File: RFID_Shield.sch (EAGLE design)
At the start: 8 parts, among them J1 ARDUINO_R3_SHIELD, Q1 MMBT2222, U1 RFID

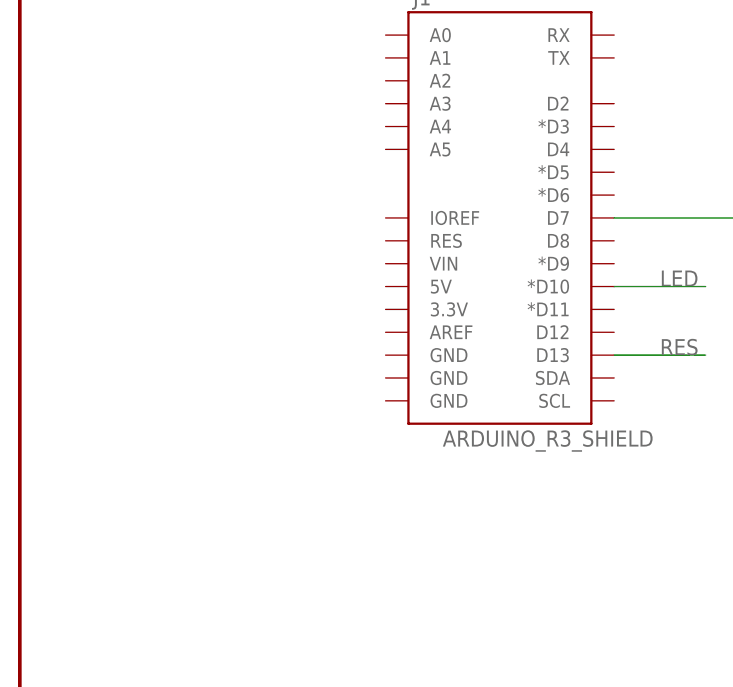
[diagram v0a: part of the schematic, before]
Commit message: Fixed missing VCC and GND connections.
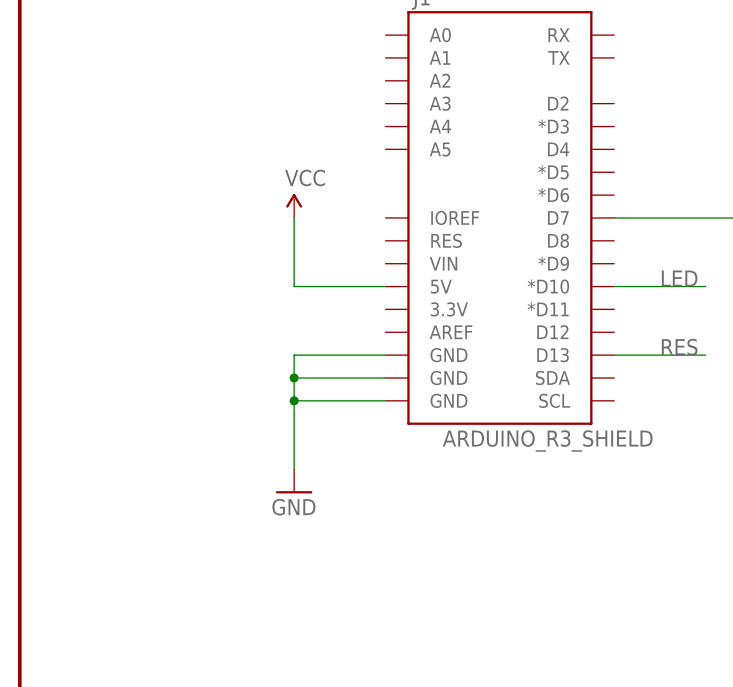
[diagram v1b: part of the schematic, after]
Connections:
- net GND: now also J1.GND@0, J1.GND@1, J1.GND@2
- net VCC: now also J1.5V
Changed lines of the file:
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@@
 <part name="GND1" library="SparkFun-Aesthetics" deviceset="GND" device=""/>
 <part name="GND2" library="SparkFun-Aesthetics" deviceset="GND" device=""/>
+<part name="SUPPLY2" library="SparkFun-Aesthetics" deviceset="VCC" device=""/>
+<part name="GND3" library="SparkFun-Aesthetics" deviceset="GND" device=""/>
 </parts>
 <sheets>
@@
 <instance part="GND1" gate="1" x="182.88" y="124.46" rot="R180"/>
 <instance part="GND2" gate="1" x="152.4" y="104.14"/>
+<instance part="SUPPLY2" gate="G$1" x="73.66" y="116.84"/>
+<instance part="GND3" gate="1" x="73.66" y="86.36"/>
 </instances>
 <busses>
@@
 <wire x1="182.88" y1="119.38" x2="182.88" y2="121.92" width="0.1524" layer="91"/>
 </segment>
+<segment>
+<pinref part="J1" gate="G$1" pin="GND@2"/>
+<pinref part="GND3" gate="1" pin="GND"/>
+<wire x1="83.82" y1="101.6" x2="73.66" y2="101.6" width="0.1524" layer="91"/>
+<wire x1="73.66" y1="101.6" x2="73.66" y2="99.06" width="0.1524" layer="91"/>
+<pinref part="J1" gate="G$1" pin="GND@1"/>
+<wire x1="73.66" y1="99.06" x2="73.66" y2="96.52" width="0.1524" layer="91"/>
+<wire x1="73.66" y1="96.52" x2="73.66" y2="88.9" width="0.1524" layer="91"/>
+<wire x1="83.82" y1="99.06" x2="73.66" y2="99.06" width="0.1524" layer="91"/>
+<junction x="73.66" y="99.06"/>
+<pinref part="J1" gate="G$1" pin="GND@0"/>
+<wire x1="83.82" y1="96.52" x2="73.66" y2="96.52" width="0.1524" layer="91"/>
+<junction x="73.66" y="96.52"/>
+</segment>
 </net>
 <net name="VCC" class="0">
@@
 <wire x1="152.4" y1="121.92" x2="152.4" y2="124.46" width="0.1524" layer="91"/>
 </segment>
+<segment>
+<pinref part="J1" gate="G$1" pin="5V"/>
+<pinref part="SUPPLY2" gate="G$1" pin="VCC"/>
+<wire x1="83.82" y1="109.22" x2="73.66" y2="109.22" width="0.1524" layer="91"/>
+<wire x1="73.66" y1="109.22" x2="73.66" y2="116.84" width="0.1524" layer="91"/>
+</segment>
 </net>
